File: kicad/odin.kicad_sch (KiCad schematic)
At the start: 0 parts

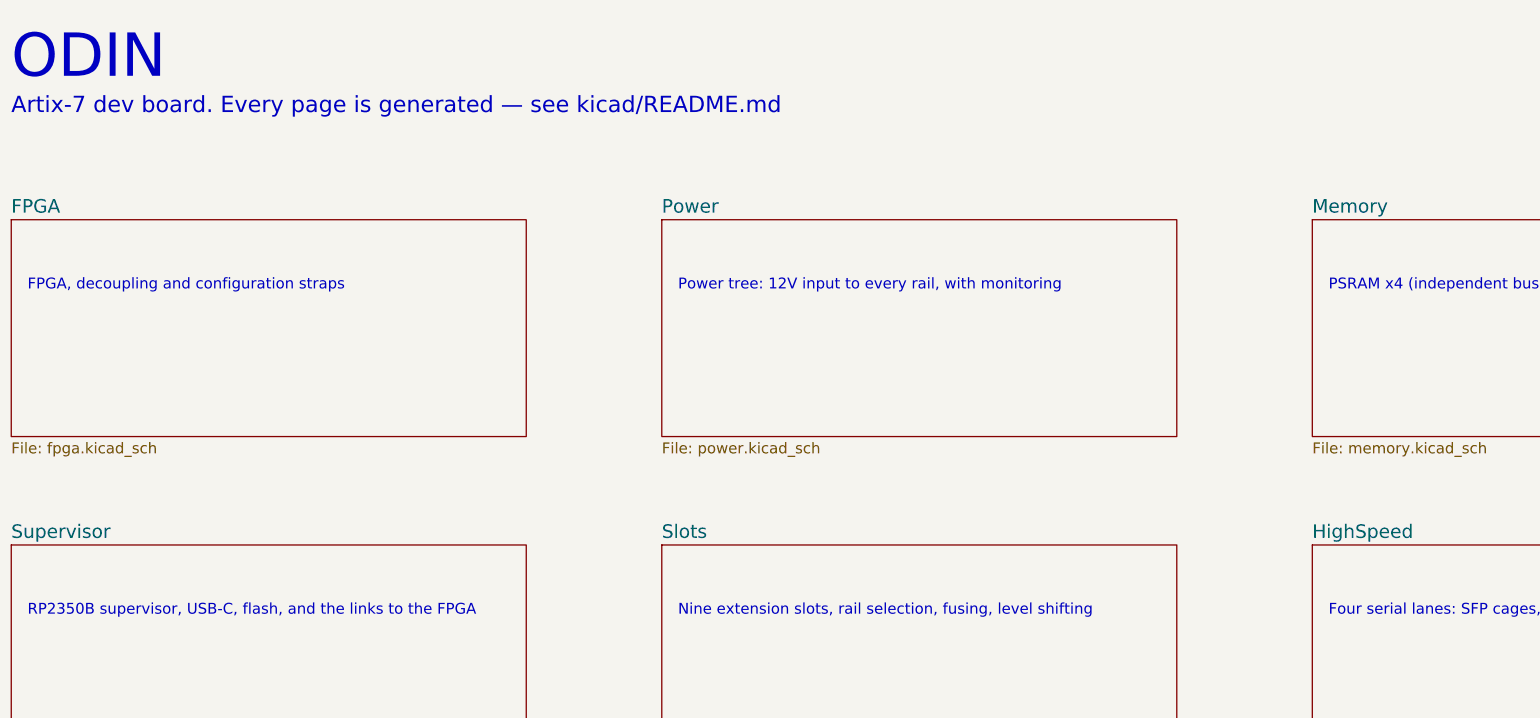
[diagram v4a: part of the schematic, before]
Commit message: Update Odin hardware design, imported parts, and documentation
Include EasyEDA symbols, footprints and 3D models; revise FPGA allocation, power and extension buses; add qualification audits and user documentation.

Validation: EasyEDA audit, qualified parts, power budget and Python syntax pass. KiCad ERC reports 1 error and 319 warnings; DRC reports 90 violations, 499 unconnected items and 209 schematic parity issues. This is a work-in-progress design snapshot. Imported vendor assets retain their original formatting.
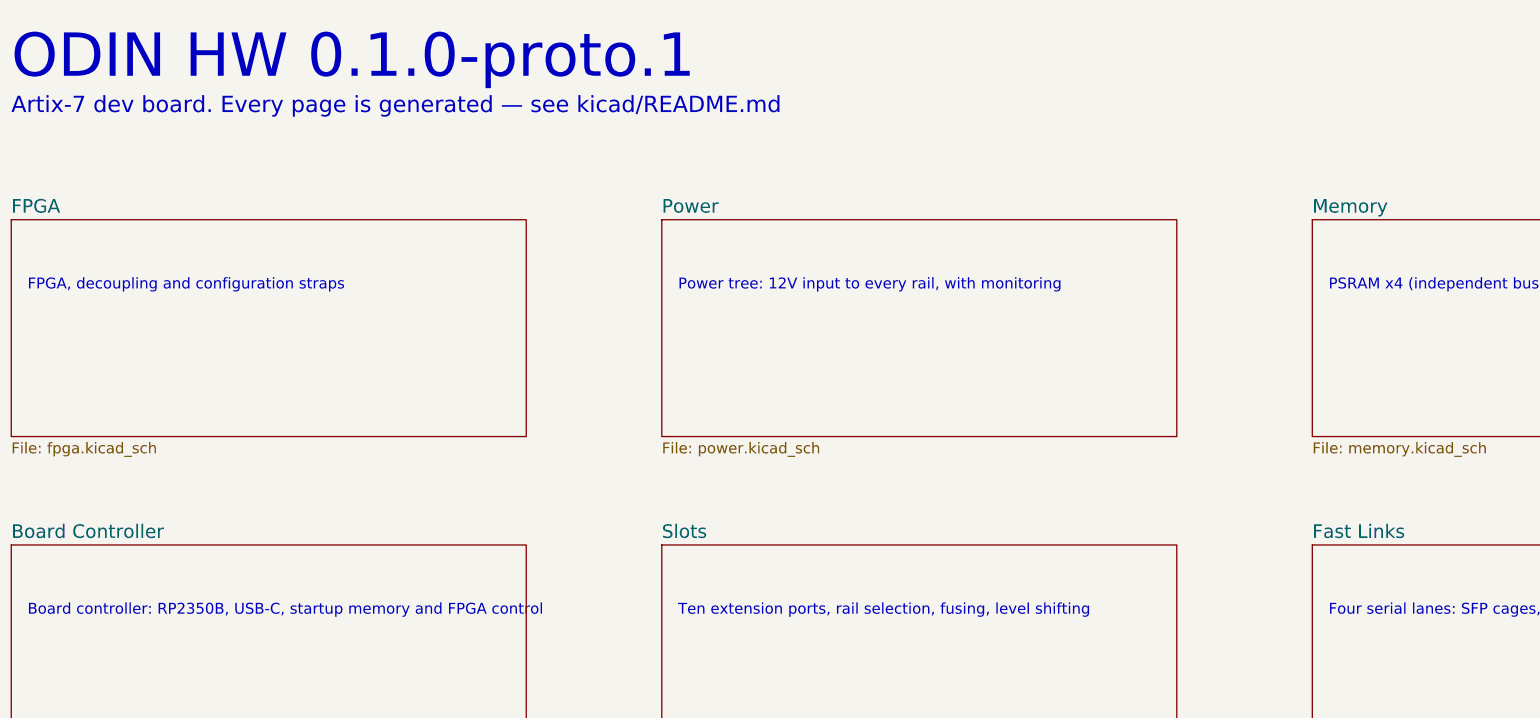
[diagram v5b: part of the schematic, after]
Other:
- sheet HighSpeed renamed Fast Links
- sheet Supervisor renamed Board Controller
- note added: "Board controller: RP2350B, USB-C, startup memory and FPGA control"
- note added: "ODIN HW 0.1.0-proto.1"
- note added: "Ten extension ports, rail selection, fusing, level shifting"
- note removed: "Nine extension slots, rail selection, fusing, level shifting"
- note removed: "ODIN"
- note removed: "RP2350B supervisor, USB-C, flash, and the links to the FPGA"
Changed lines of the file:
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@@
 	(generator_version "9.0")
 	(paper "A3")
-	(text "ODIN" (at 30 25 0) (effects (font (size 8 8) (thickness 1.2)) (justify left)))
+	(text "ODIN HW 0.1.0-proto.1" (at 30 25 0) (effects (font (size 8 8) (thickness 1.2)) (justify left)))
 	(text "Artix-7 dev board. Every page is generated — see kicad/README.md" (at 30 34 0) (effects (font (size 3 3)) (justify left)))
 	(sheet (at 30 55) (size 95 40)
@@
 	(sheet (at 30 115) (size 95 40)
 		(stroke (width 0.1524) (type solid)) (fill (color 0 0 0 0.0000))
-		(property "Sheetname" "Supervisor" (at 30 114 0) (effects (font (size 2.5 2.5)) (justify left bottom)))
+		(property "Sheetname" "Board Controller" (at 30 114 0) (effects (font (size 2.5 2.5)) (justify left bottom)))
 		(property "Sheetfile" "supervisor.kicad_sch" (at 30 156 0) (effects (font (size 2 2)) (justify left top)))
 		(instances (project "odin" (path "/c44fb7fe-6133-ad34-68fd-fb66126197ef" (page "5"))))
 	)
-	(text "RP2350B supervisor, USB-C, flash, and the links to the FPGA" (at 33 127 0) (effects (font (size 2 2)) (justify left)))
+	(text "Board controller: RP2350B, USB-C, startup memory and FPGA control" (at 33 127 0) (effects (font (size 2 2)) (justify left)))
 	(sheet (at 150 115) (size 95 40)
 		(stroke (width 0.1524) (type solid)) (fill (color 0 0 0 0.0000))
@@
 		(instances (project "odin" (path "/c44fb7fe-6133-ad34-68fd-fb66126197ef" (page "6"))))
 	)
-	(text "Nine extension slots, rail selection, fusing, level shifting" (at 153 127 0) (effects (font (size 2 2)) (justify left)))
+	(text "Ten extension ports, rail selection, fusing, level shifting" (at 153 127 0) (effects (font (size 2 2)) (justify left)))
 	(sheet (at 270 115) (size 95 40)
 		(stroke (width 0.1524) (type solid)) (fill (color 0 0 0 0.0000))
-		(property "Sheetname" "HighSpeed" (at 270 114 0) (effects (font (size 2.5 2.5)) (justify left bottom)))
+		(property "Sheetname" "Fast Links" (at 270 114 0) (effects (font (size 2.5 2.5)) (justify left bottom)))
 		(property "Sheetfile" "highspeed.kicad_sch" (at 270 156 0) (effects (font (size 2 2)) (justify left top)))
 		(instances (project "odin" (path "/c44fb7fe-6133-ad34-68fd-fb66126197ef" (page "7"))))

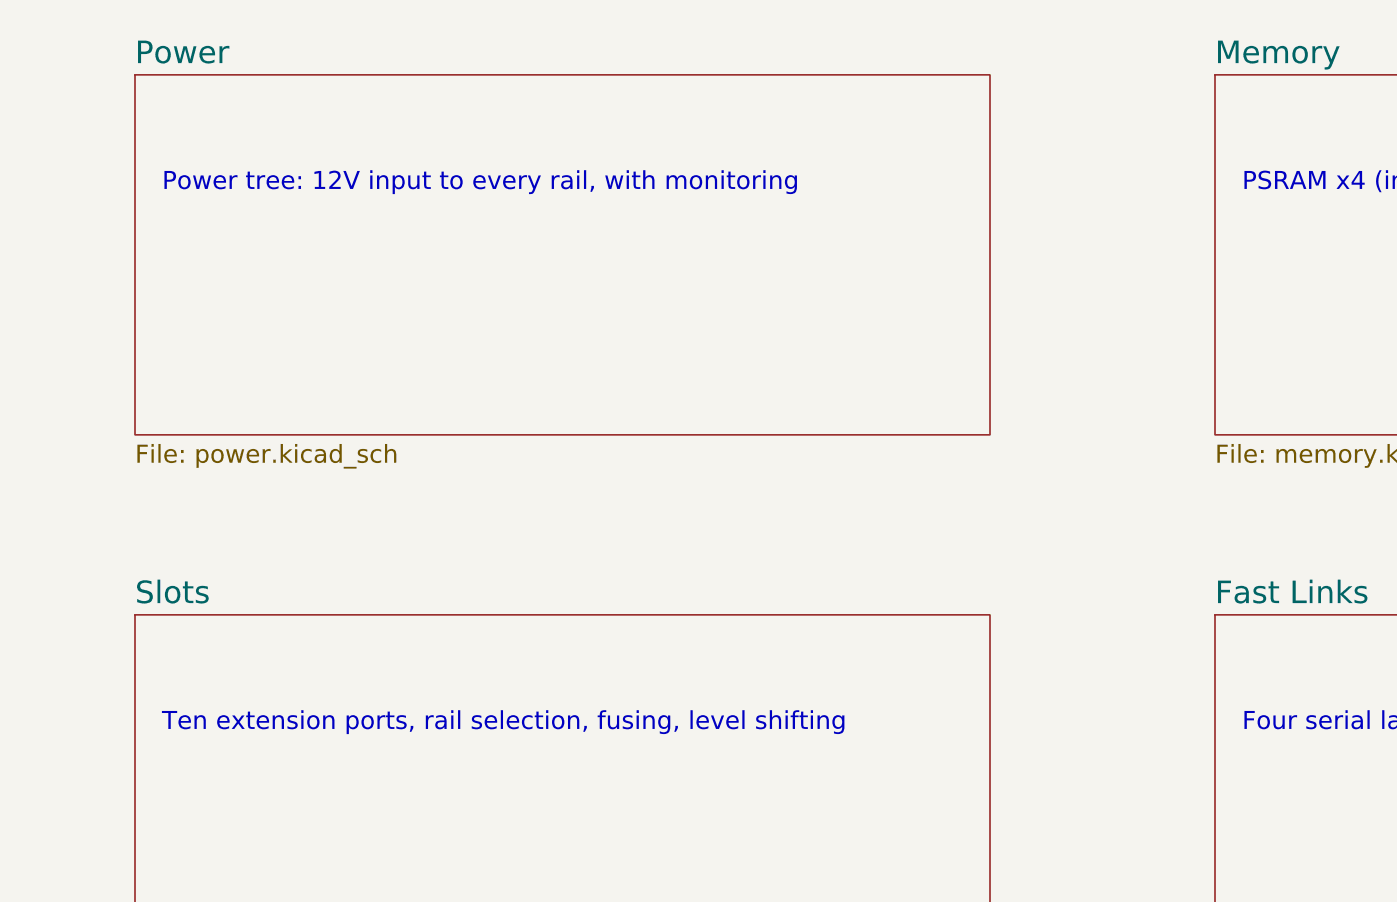
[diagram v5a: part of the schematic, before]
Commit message: Through-hole extension headers, AUX supply rework, and board state before rev A cleanup
J3/J5 become single 2x32 through-hole bodies with IO IO GND rows and a long
grounded key post per zone. Power sheet reworked around the AUX rail.
Decoupling moved off B.Cu. New footprints, 3D models and check scripts.
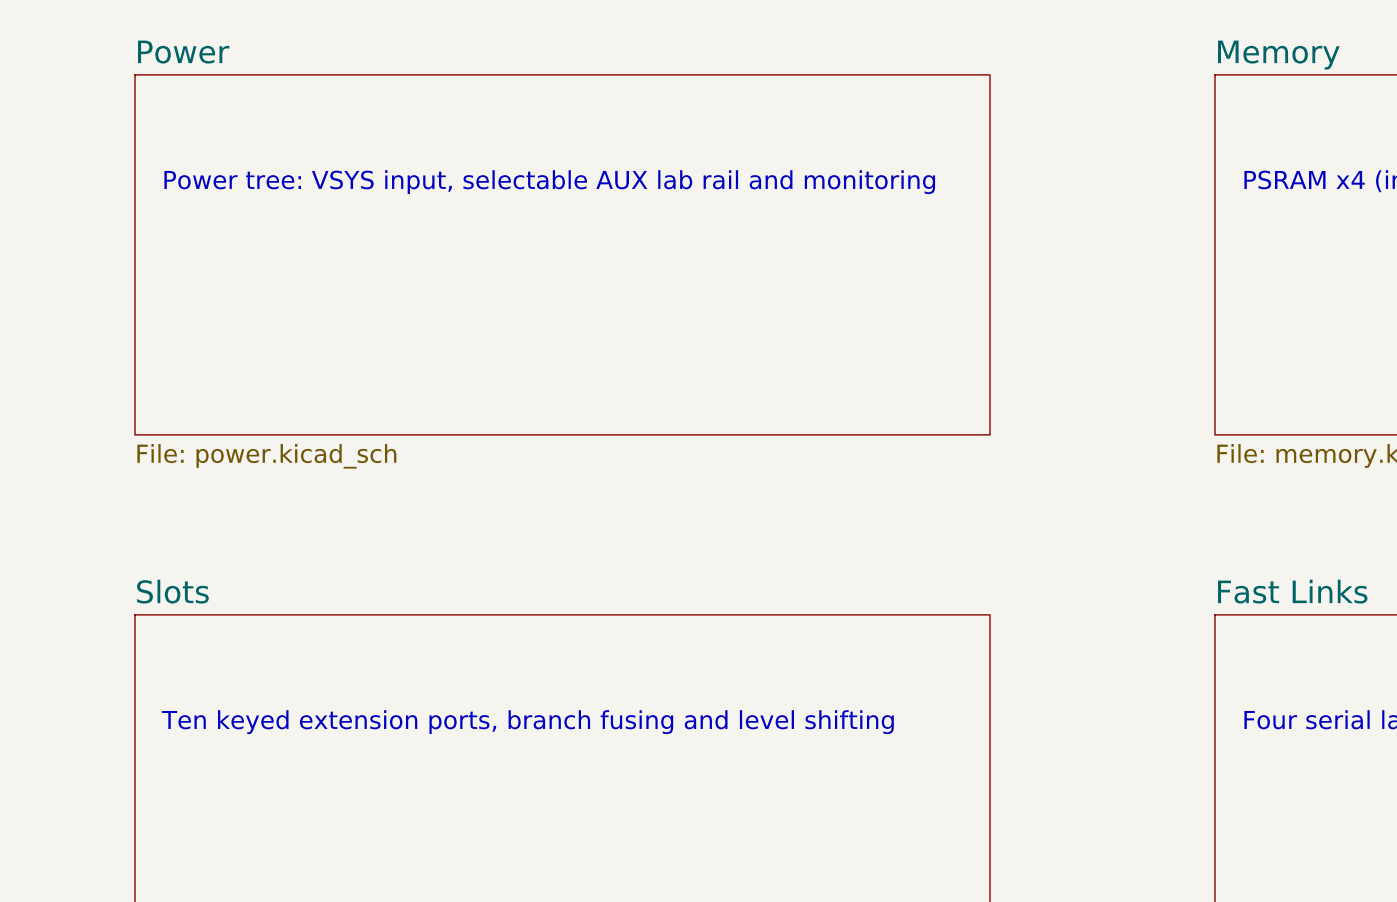
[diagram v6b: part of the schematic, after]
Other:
- note added: "Power tree: VSYS input, selectable AUX lab rail and monitoring"
- note added: "Ten keyed extension ports, branch fusing and level shifting"
- note removed: "Power tree: 12V input to every rail, with monitoring"
- note removed: "Ten extension ports, rail selection, fusing, level shifting"
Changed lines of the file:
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@@
 		(instances (project "odin" (path "/c44fb7fe-6133-ad34-68fd-fb66126197ef" (page "3"))))
 	)
-	(text "Power tree: 12V input to every rail, with monitoring" (at 153 67 0) (effects (font (size 2 2)) (justify left)))
+	(text "Power tree: VSYS input, selectable AUX lab rail and monitoring" (at 153 67 0) (effects (font (size 2 2)) (justify left)))
 	(sheet (at 270 55) (size 95 40)
 		(stroke (width 0.1524) (type solid)) (fill (color 0 0 0 0.0000))
@@
 		(instances (project "odin" (path "/c44fb7fe-6133-ad34-68fd-fb66126197ef" (page "6"))))
 	)
-	(text "Ten extension ports, rail selection, fusing, level shifting" (at 153 127 0) (effects (font (size 2 2)) (justify left)))
+	(text "Ten keyed extension ports, branch fusing and level shifting" (at 153 127 0) (effects (font (size 2 2)) (justify left)))
 	(sheet (at 270 115) (size 95 40)
 		(stroke (width 0.1524) (type solid)) (fill (color 0 0 0 0.0000))

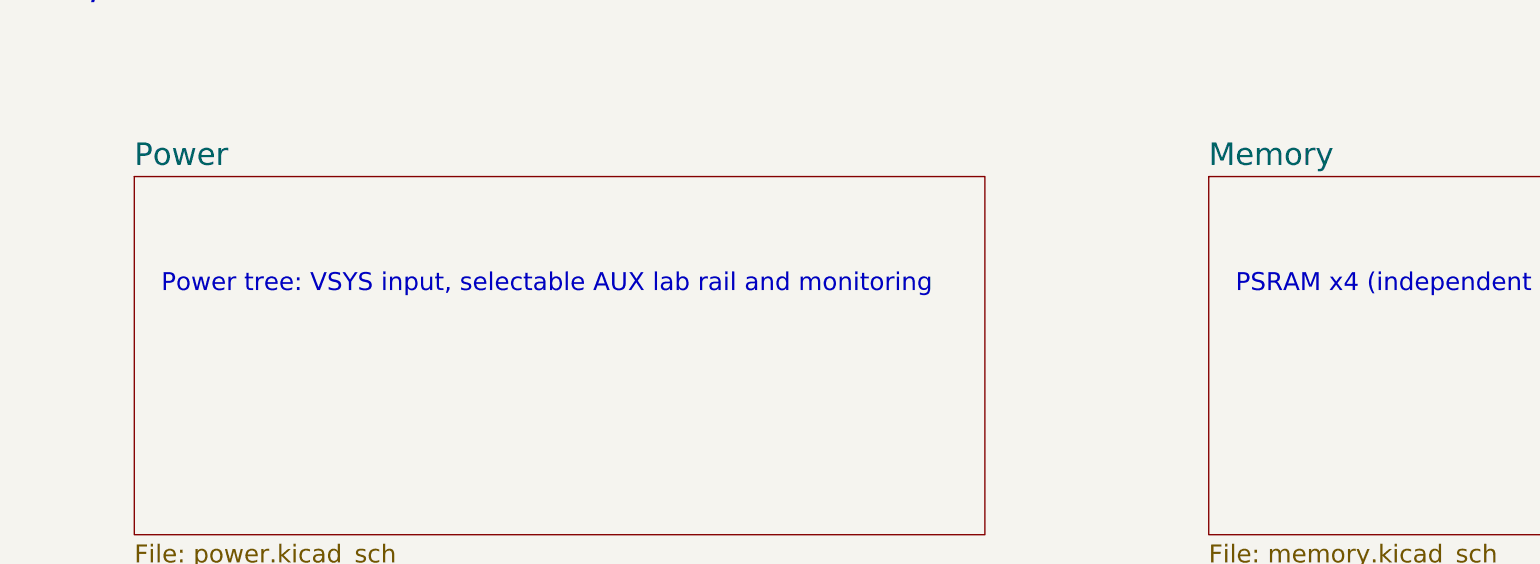
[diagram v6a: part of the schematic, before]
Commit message: Remove the AUX lab rail: J68 feeds AUX_RAIL straight into the ten branch PTCs
Decision D1 of the rev A plan. The LM5157 SEPIC (U28, L10, D12), the
cap-selected 9/12/15/24 V feedback ladder (J67, U29, Q5-Q8, D13-D16) and
the REG/AUX/RAW source selector J66 are gone, 43 parts in all. The AUX
pin of every power row is now fed only from the AUX IN screw terminal
through its slot's 33 V PTC. The SMBJ22A clamp plus a charged 24 V
output could exceed the LM5157 SW pin's 50 V absolute maximum, and the
converter is not needed for a board that configures and runs.

budget.py drops the SEPIC derating math and the surge release hold;
qualified.py, gen_kicad.py, gen_project.py, the connector checker, the
silkscreen labels and the power docs follow. PCB synced with load_pcb.py,
0 of 477 footprints moved; DRC errors 49 -> 18.
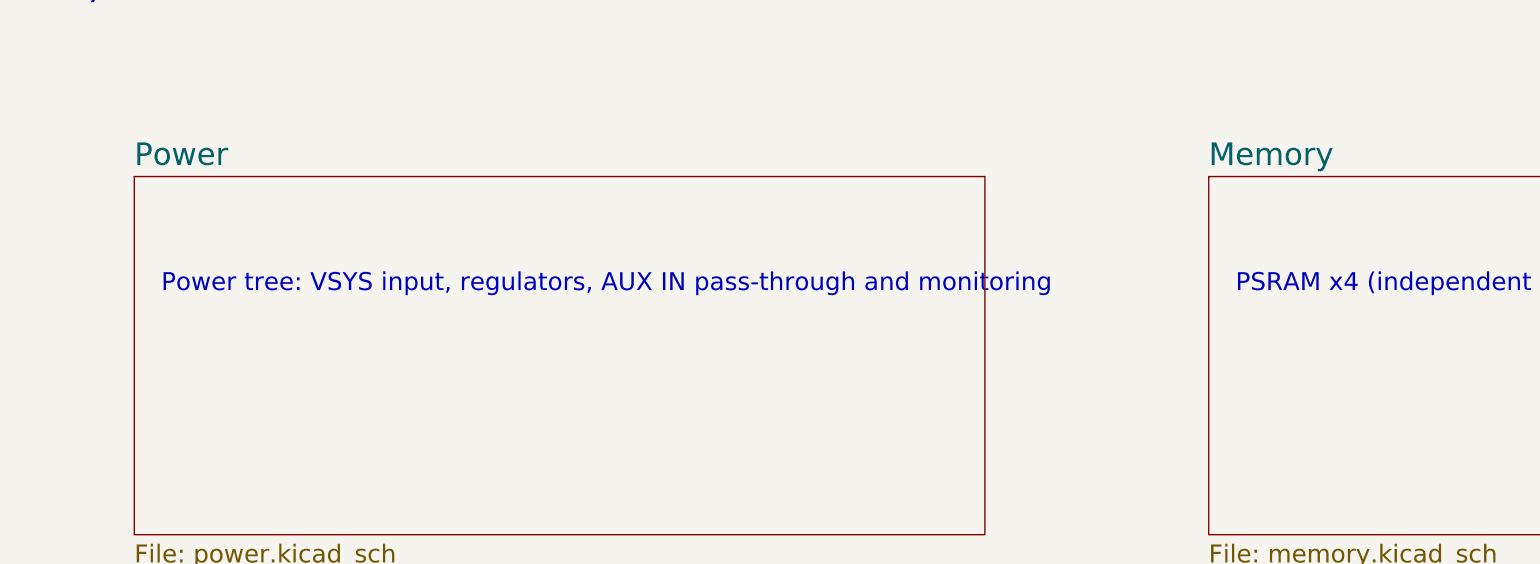
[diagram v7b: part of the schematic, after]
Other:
- note added: "Power tree: VSYS input, regulators, AUX IN pass-through and monitoring"
- note removed: "Power tree: VSYS input, selectable AUX lab rail and monitoring"
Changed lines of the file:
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@@
 		(instances (project "odin" (path "/c44fb7fe-6133-ad34-68fd-fb66126197ef" (page "3"))))
 	)
-	(text "Power tree: VSYS input, selectable AUX lab rail and monitoring" (at 153 67 0) (effects (font (size 2 2)) (justify left)))
+	(text "Power tree: VSYS input, regulators, AUX IN pass-through and monitoring" (at 153 67 0) (effects (font (size 2 2)) (justify left)))
 	(sheet (at 270 55) (size 95 40)
 		(stroke (width 0.1524) (type solid)) (fill (color 0 0 0 0.0000))
